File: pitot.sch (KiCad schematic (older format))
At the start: 15 parts, among them IC1 LT1167CN8PBF, IC2 LT1167CN8PBF, IC3 LT1167CN8PBF, IC4 LTC1144CN8#PBF, IC5 DEV-11114, P1 DIL8, P2 DIL8, P3 DIL8, P4 CONN_01X04, U1 LM7809CT

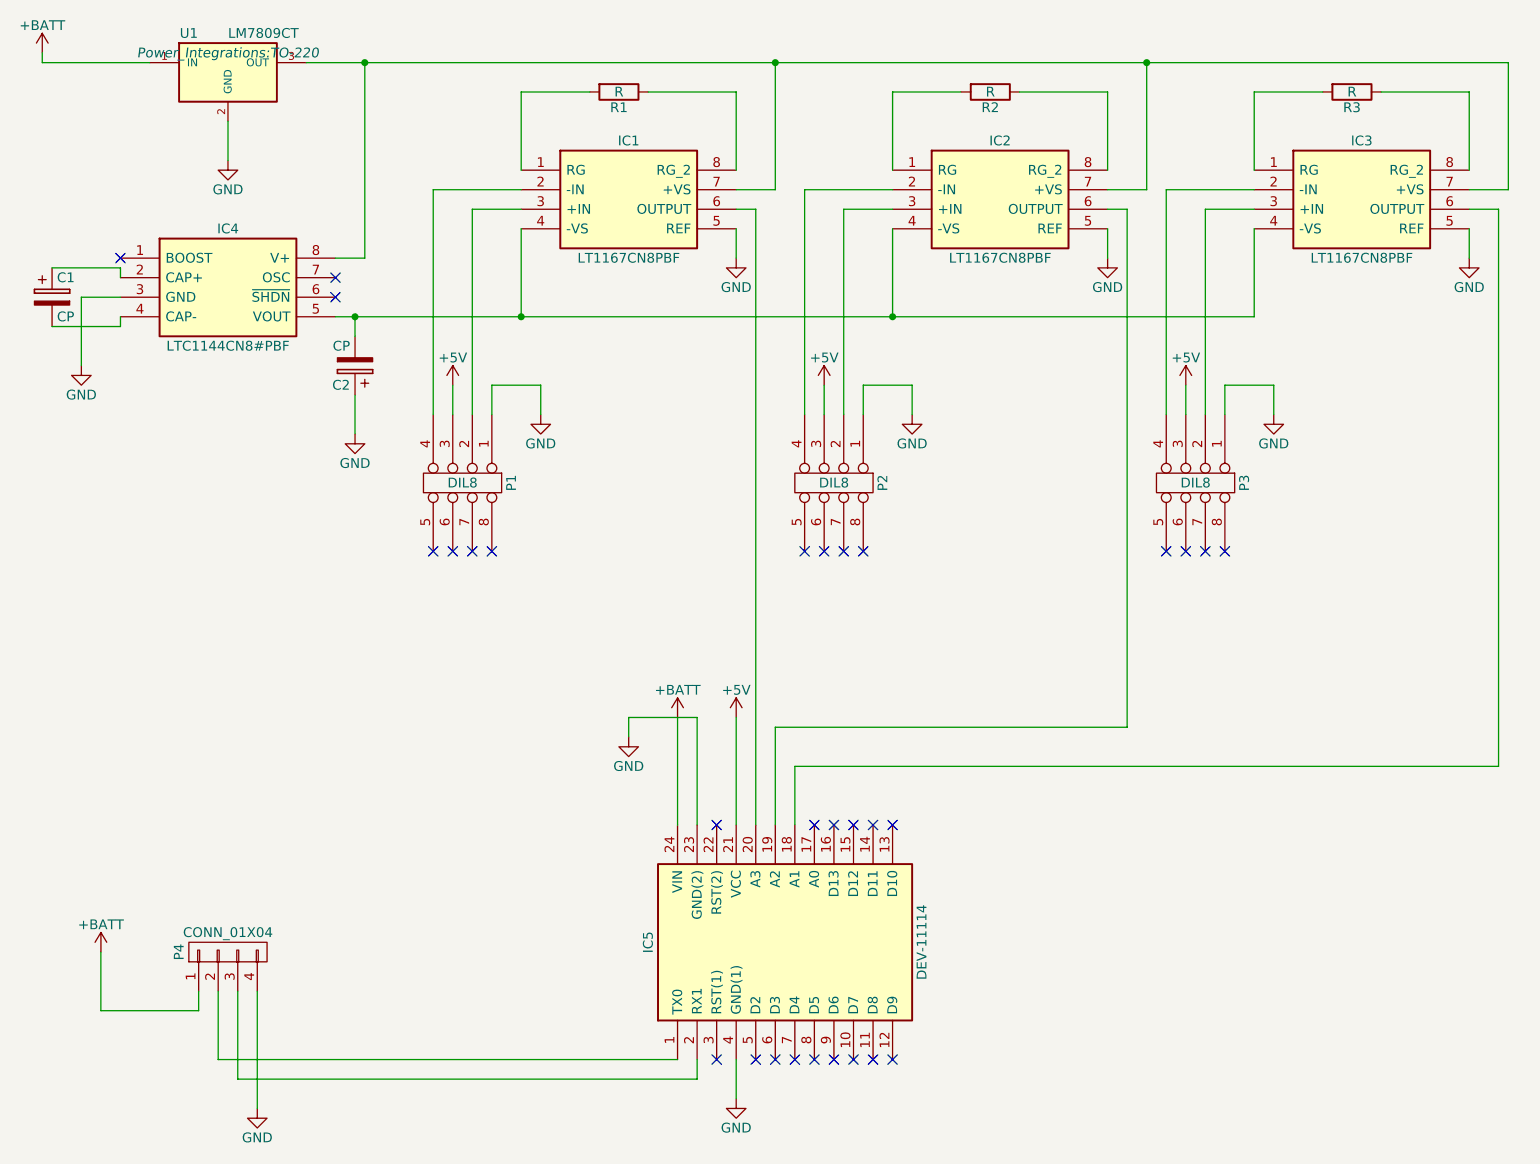
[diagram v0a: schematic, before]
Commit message: add ZD and LPF
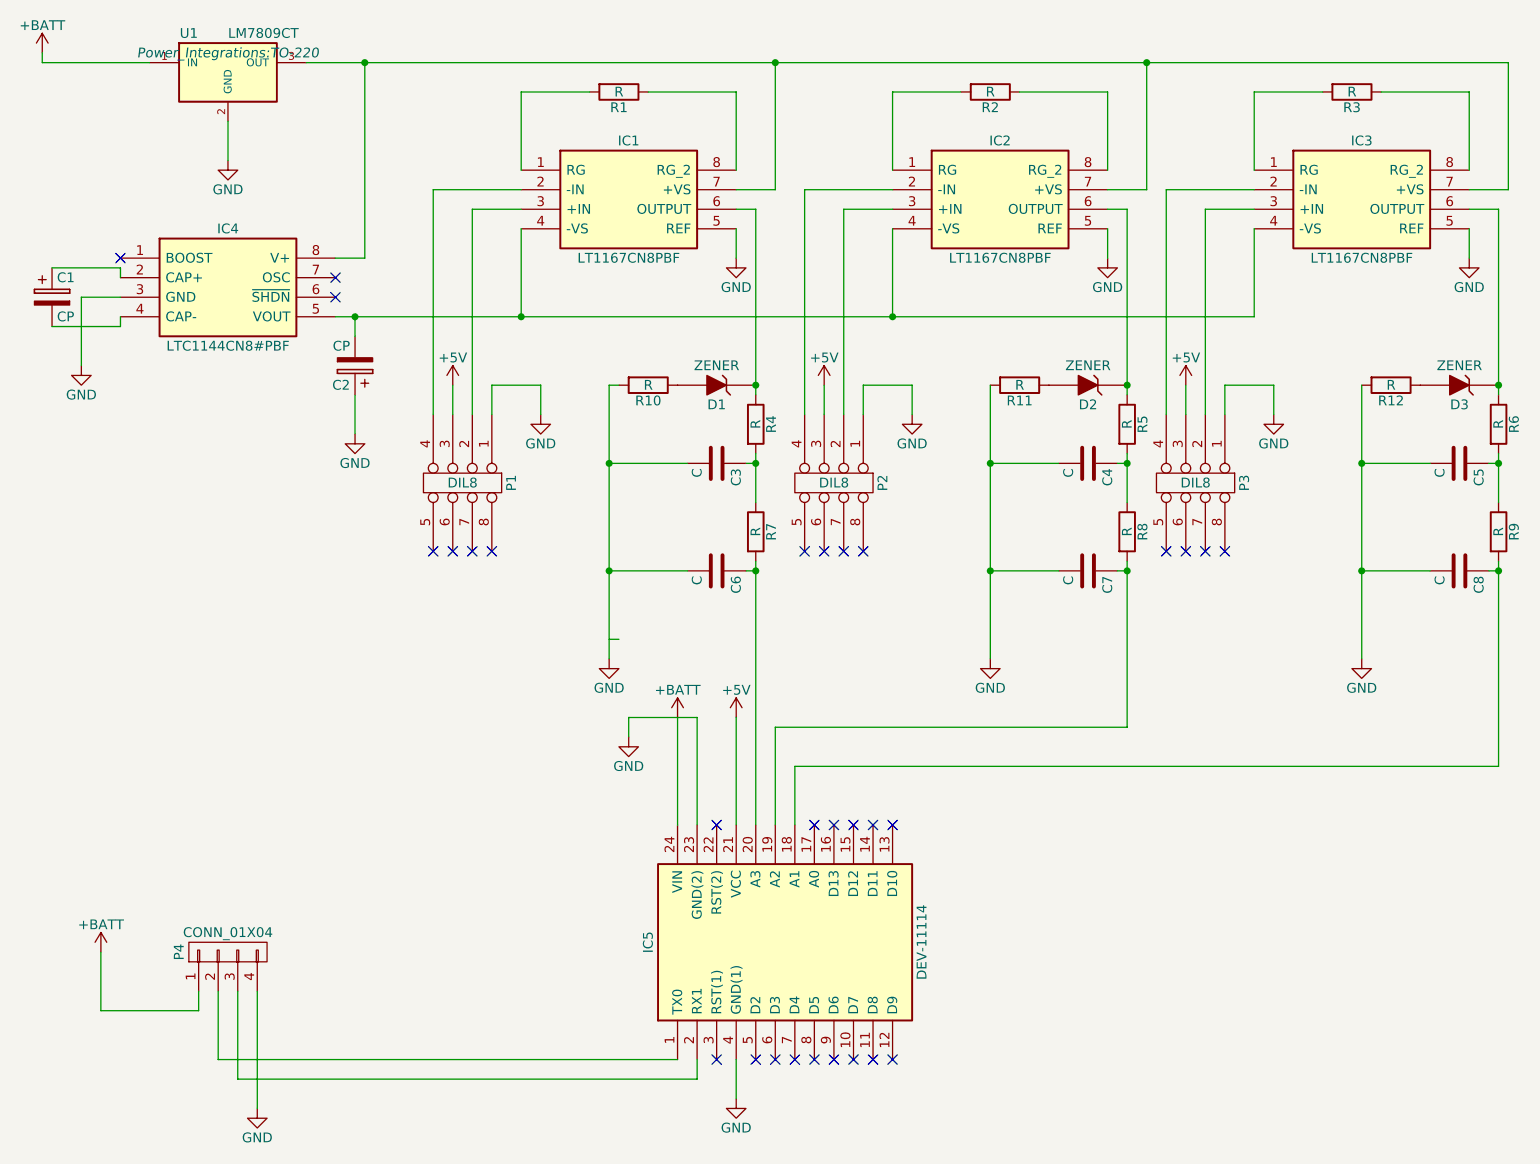
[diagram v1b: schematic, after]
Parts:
- added C3, C4, C5, C6, C7, C8: C, Capacitors_ThroughHole:C_Disc_D3.0mm_W1.6mm_P2.50mm, symbol C
- added D1, D2, D3: ZENER, Discret:D3, symbol ZENER
- added R10, R11, R12: R, Resistors_ThroughHole:R_Axial_DIN0204_L3.6mm_D1.6mm_P5.08mm_Horizontal, symbol R
- added R4, R5, R6, R7, R8, R9: R, Resistors_ThroughHole:R_Axial_DIN0204_L3.6mm_D1.6mm_P1.90mm_Vertical, symbol R
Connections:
- net GND: now also C3.2, C4.2, C5.2, C6.2, C7.2, C8.2, R10.2, R11.2, R12.2
- net at IC1.6 (OUTPUT): now also D1.1 (K), R4.1; no longer IC5.20 (A3)
- net at IC5.18 (A1): now also C8.1, R9.2; no longer IC3.6 (OUTPUT)
- net at IC5.19 (A2): now also C7.1, R8.2; no longer IC2.6 (OUTPUT)
- new net: C6.1, IC5.20 (A3), R7.2
- new net: D2.1 (K), IC2.6 (OUTPUT), R5.1
- new net: D3.1 (K), IC3.6 (OUTPUT), R6.1
- new net: D1.2 (A), R10.1
- new net: C3.1, R4.2, R7.1
- new net: D2.2 (A), R11.1
- new net: C4.1, R5.2, R8.1
- new net: D3.2 (A), R12.1
- new net: C5.1, R6.2, R9.1

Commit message: mod pcb layout
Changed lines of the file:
@@
 	0    1    1    0
 $EndComp
-Wire Wire Line
-	6300 3850 6250 3850
 $Comp
 L R R11
